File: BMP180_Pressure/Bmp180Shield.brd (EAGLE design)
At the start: 39.7 x 26.7 mm, 5 parts

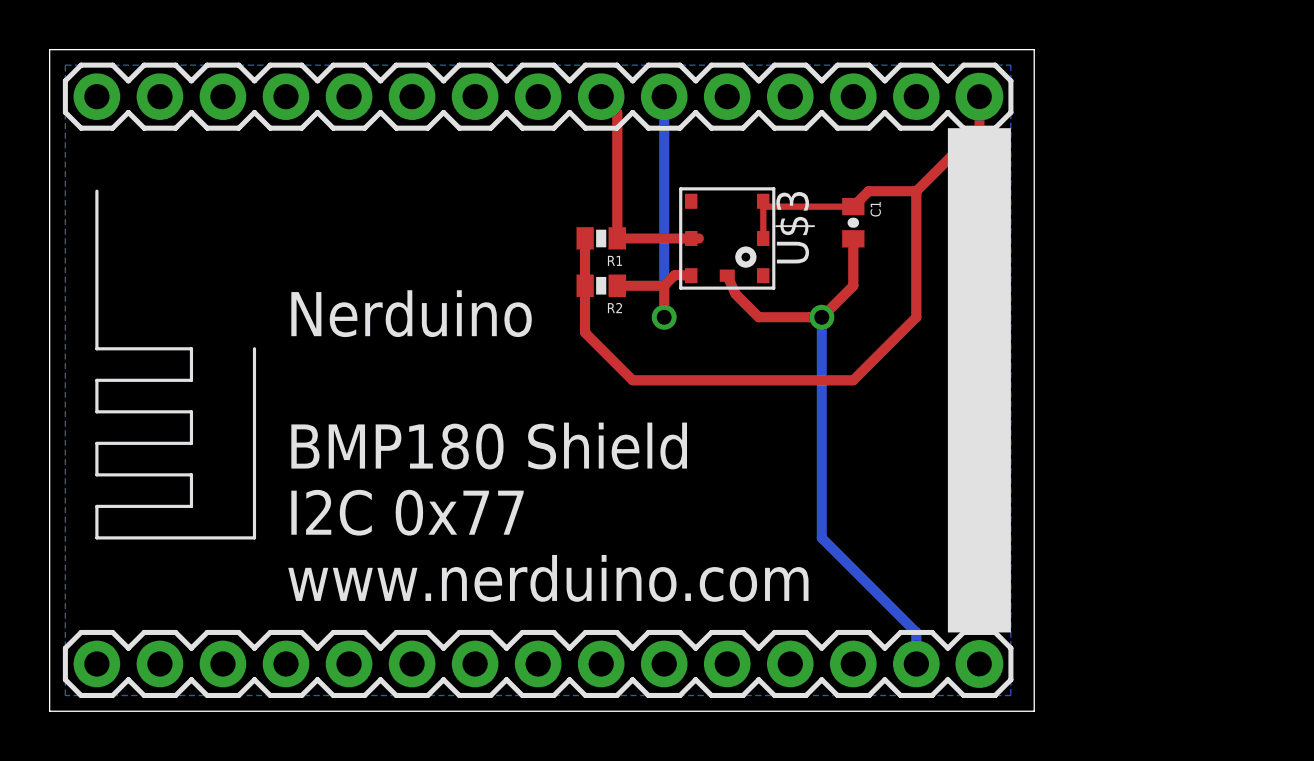
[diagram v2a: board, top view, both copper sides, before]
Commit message: Added OLED Shield Added LiPo Battery Charger Shield Updated outlines of all shields to match the cutout of the nodemcu board
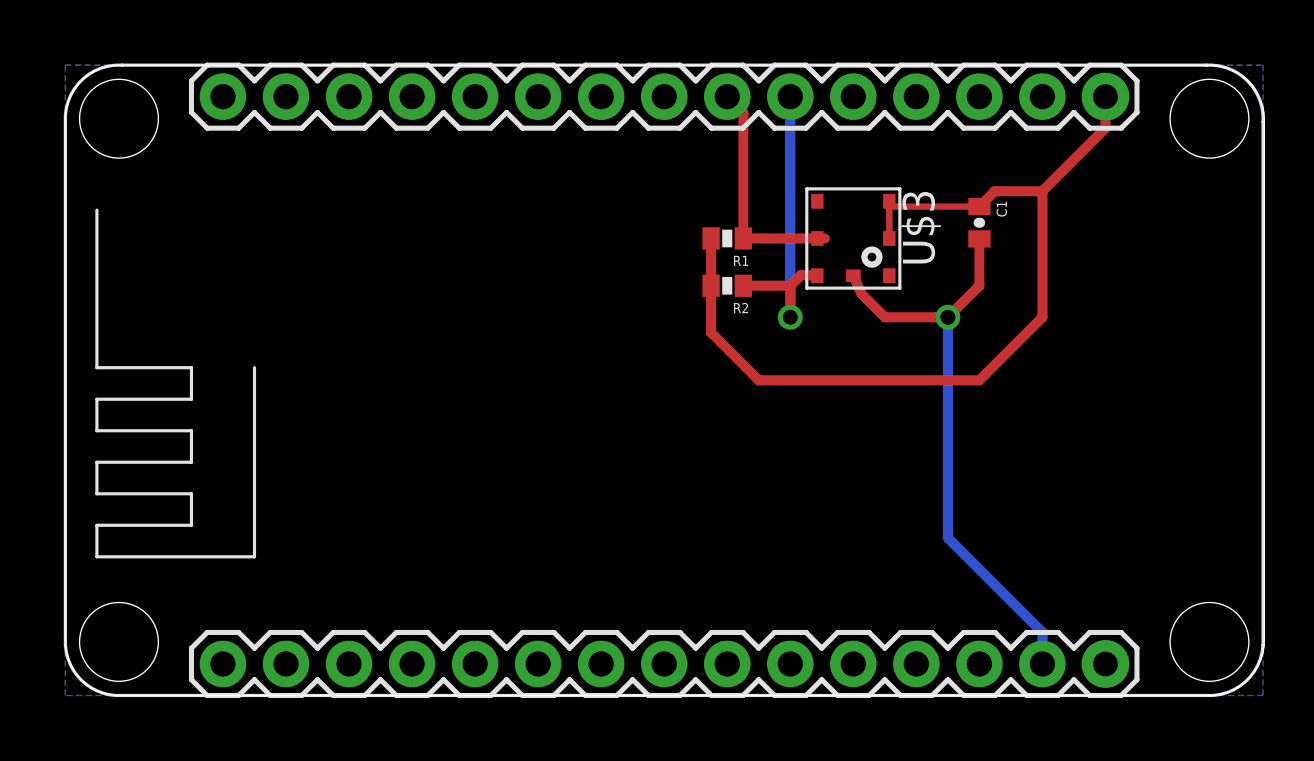
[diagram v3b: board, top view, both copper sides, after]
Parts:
- moved R1 5.08 mm to (26.7, 18.4)
- moved R2 5.08 mm to (26.7, 16.5)
- moved C1 5.08 mm to (36.8, 19.1)
- moved U$1 5.08 mm to (24.1, 6.35)
- moved U$3 5.08 mm to (31.8, 18.4)
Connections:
- net GND: now also U$1.10, U$1.17, U$1.24
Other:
- board size 39.7 x 26.7 mm -> 48.3 x 25.4 mm
- board text added: "NERDUINO BMP180 Shield I2C 0x77 www.nerduino.com"
- board text removed: "Nerduino BMP180 Shield I2C 0x77 www.nerduino.com"
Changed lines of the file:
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@@
 <setting verticaltext="up"/>
 </settings>
-<grid distance="0.025" unitdist="inch" unit="inch" style="lines" multiple="1" display="no" altdistance="0.0125" altunitdist="inch" altunit="inch"/>
+<grid distance="0.005" unitdist="inch" unit="inch" style="lines" multiple="1" display="no" altdistance="0.0125" altunitdist="inch" altunit="inch"/>
 <layers>
 <layer number="1" name="Top" color="4" fill="1" visible="yes" active="yes"/>
@@
 <board>
 <plain>
-<wire x1="-0.635" y1="-0.635" x2="39.04" y2="-0.635" width="0" layer="20"/>
-<wire x1="39.04" y1="-0.635" x2="39.04" y2="26.025" width="0" layer="20"/>
-<wire x1="39.04" y1="26.025" x2="-0.635" y2="26.025" width="0" layer="20"/>
-<wire x1="-0.635" y1="26.025" x2="-0.635" y2="-0.635" width="0" layer="20"/>
-<text x="8.89" y="3.81" size="1.778" layer="121">Nerduino
+<wire x1="0" y1="23.237253125" x2="0" y2="2.1849875" width="0" layer="20"/>
+<wire x1="0" y1="2.1849875" x2="2.1849875" y2="0" width="0" layer="20" curve="90"/>
+<wire x1="2.1849875" y1="0" x2="46.0843125" y2="0" width="0" layer="20"/>
+<wire x1="46.0843125" y1="0" x2="48.311" y2="2.2266875" width="0" layer="20" curve="90"/>
+<wire x1="48.311" y1="2.2266875" x2="48.311" y2="23.205321875" width="0" layer="20"/>
+<wire x1="48.311" y1="23.205321875" x2="46.126321875" y2="25.39" width="0" layer="20" curve="90"/>
+<wire x1="46.126321875" y1="25.39" x2="2.152746875" y2="25.39" width="0" layer="20"/>
+<wire x1="2.152746875" y1="25.39" x2="0" y2="23.237253125" width="0" layer="20" curve="90"/>
+<text x="32.385" y="3.683" size="1.778" layer="122" rot="MR0">NERDUINO
 BMP180 Shield
 I2C 0x77
@@
 </autorouter>
 <elements>
-<element name="C1" library="SparkFun" package="0402-CAP" value="0.1uF" x="31.75" y="19.05" rot="R270"/>
-<element name="R1" library="SparkFun" package="0402-RES" value="4.7k" x="21.59" y="18.415" rot="R180"/>
-<element name="R2" library="SparkFun" package="0402-RES" value="4.7k" x="21.59" y="16.51" rot="R180"/>
-<element name="U$1" library="NerduinoShieldLib" package="NERDUINO_STACK" value="NERDSHIELD" x="19.05" y="6.35"/>
-<element name="U$3" library="SparkFun-Sensors" package="BMP180" value="BMP180" x="26.67" y="18.415" rot="R270"/>
+<element name="C1" library="SparkFun" package="0402-CAP" value="0.1uF" x="36.83" y="19.05" rot="R270"/>
+<element name="R1" library="SparkFun" package="0402-RES" value="4.7k" x="26.67" y="18.415" rot="R180"/>
+<element name="R2" library="SparkFun" package="0402-RES" value="4.7k" x="26.67" y="16.51" rot="R180"/>
+<element name="U$1" library="NerduinoShieldLib" package="NERDUINO_STACK" value="NERDSHIELD" x="24.13" y="6.35"/>
+<element name="U$3" library="SparkFun-Sensors" package="BMP180" value="BMP180" x="31.75" y="18.415" rot="R270"/>
 </elements>
 <signals>
@@
 <polygon width="0.4064" layer="16">
 <vertex x="0" y="25.4"/>
-<vertex x="38.1" y="25.4"/>
-<vertex x="38.1" y="0"/>
+<vertex x="48.26" y="25.4"/>
+<vertex x="48.26" y="0"/>
 <vertex x="0" y="0"/>
 </polygon>
-<wire x1="31.75" y1="18.4" x2="31.75" y2="16.51" width="0.4064" layer="1"/>
-<wire x1="31.75" y1="16.51" x2="30.48" y2="15.24" width="0.4064" layer="1"/>
-<wire x1="30.48" y1="15.24" x2="30.005" y2="15.24" width="0.4064" layer="1"/>
-<via x="30.48" y="15.24" extent="1-16" drill="0.6" shape="square"/>
-<wire x1="30.48" y1="15.24" x2="30.48" y2="6.35" width="0.4064" layer="16"/>
-<wire x1="30.48" y1="6.35" x2="34.29" y2="2.54" width="0.4064" layer="16"/>
-<wire x1="34.29" y1="2.54" x2="34.29" y2="1.27" width="0.4064" layer="16"/>
+<wire x1="36.83" y1="18.4" x2="36.83" y2="16.51" width="0.4064" layer="1"/>
+<wire x1="36.83" y1="16.51" x2="35.56" y2="15.24" width="0.4064" layer="1"/>
+<wire x1="35.56" y1="15.24" x2="35.085" y2="15.24" width="0.4064" layer="1"/>
+<via x="35.56" y="15.24" extent="1-16" drill="0.6" shape="square"/>
+<wire x1="35.56" y1="15.24" x2="35.56" y2="6.35" width="0.4064" layer="16"/>
+<wire x1="35.56" y1="6.35" x2="39.37" y2="2.54" width="0.4064" layer="16"/>
+<wire x1="39.37" y1="2.54" x2="39.37" y2="1.27" width="0.4064" layer="16"/>
 <contactref element="U$3" pad="7"/>
-<wire x1="26.67" y1="16.915" x2="27.005" y2="16.175" width="0.4064" layer="1"/>
-<wire x1="27.005" y1="16.175" x2="27.94" y2="15.24" width="0.4064" layer="1"/>
-<wire x1="27.94" y1="15.24" x2="30.48" y2="15.24" width="0.4064" layer="1"/>
+<wire x1="31.75" y1="16.915" x2="32.085" y2="16.175" width="0.4064" layer="1"/>
+<wire x1="32.085" y1="16.175" x2="33.02" y2="15.24" width="0.4064" layer="1"/>
+<wire x1="33.02" y1="15.24" x2="35.56" y2="15.24" width="0.4064" layer="1"/>
+<contactref element="U$1" pad="10"/>
+<contactref element="U$1" pad="17"/>
+<contactref element="U$1" pad="24"/>
 </signal>
 <signal name="3.3V">
@@
 <contactref element="R2" pad="2"/>
 <contactref element="R1" pad="2"/>
-<wire x1="36.83" y1="24.13" x2="36.83" y2="22.86" width="0.4064" layer="1"/>
-<wire x1="36.83" y1="22.86" x2="34.29" y2="20.32" width="0.4064" layer="1"/>
-<wire x1="34.29" y1="20.32" x2="32.37" y2="20.32" width="0.4064" layer="1"/>
-<wire x1="32.37" y1="20.32" x2="31.75" y2="19.7" width="0.4064" layer="1"/>
-<wire x1="20.94" y1="18.415" x2="20.94" y2="16.51" width="0.4064" layer="1"/>
-<wire x1="20.94" y1="16.51" x2="20.94" y2="14.62" width="0.4064" layer="1"/>
-<wire x1="20.94" y1="14.62" x2="22.86" y2="12.7" width="0.4064" layer="1"/>
-<wire x1="22.86" y1="12.7" x2="31.75" y2="12.7" width="0.4064" layer="1"/>
-<wire x1="31.75" y1="12.7" x2="34.29" y2="15.24" width="0.4064" layer="1"/>
-<wire x1="34.29" y1="15.24" x2="34.29" y2="20.32" width="0.4064" layer="1"/>
+<wire x1="41.91" y1="24.13" x2="41.91" y2="22.86" width="0.4064" layer="1"/>
+<wire x1="41.91" y1="22.86" x2="39.37" y2="20.32" width="0.4064" layer="1"/>
+<wire x1="39.37" y1="20.32" x2="37.45" y2="20.32" width="0.4064" layer="1"/>
+<wire x1="37.45" y1="20.32" x2="36.83" y2="19.7" width="0.4064" layer="1"/>
+<wire x1="26.02" y1="18.415" x2="26.02" y2="16.51" width="0.4064" layer="1"/>
+<wire x1="26.02" y1="16.51" x2="26.02" y2="14.62" width="0.4064" layer="1"/>
+<wire x1="26.02" y1="14.62" x2="27.94" y2="12.7" width="0.4064" layer="1"/>
+<wire x1="27.94" y1="12.7" x2="36.83" y2="12.7" width="0.4064" layer="1"/>
+<wire x1="36.83" y1="12.7" x2="39.37" y2="15.24" width="0.4064" layer="1"/>
+<wire x1="39.37" y1="15.24" x2="39.37" y2="20.32" width="0.4064" layer="1"/>
 <contactref element="U$3" pad="2"/>
 <contactref element="U$3" pad="3"/>
-<wire x1="31.75" y1="19.7" x2="28.12" y2="19.7" width="0.254" layer="1"/>
-<wire x1="28.12" y1="19.7" x2="28.12" y2="19.915" width="0.254" layer="1"/>
-<wire x1="28.12" y1="19.915" x2="28.12" y2="18.415" width="0.254" layer="1"/>
+<wire x1="36.83" y1="19.7" x2="33.2" y2="19.7" width="0.254" layer="1"/>
+<wire x1="33.2" y1="19.7" x2="33.2" y2="19.915" width="0.254" layer="1"/>
+<wire x1="33.2" y1="19.915" x2="33.2" y2="18.415" width="0.254" layer="1"/>
 </signal>
 <signal name="N$2">
 <contactref element="R2" pad="1"/>
 <contactref element="U$1" pad="21"/>
-<wire x1="24.13" y1="16.51" x2="22.24" y2="16.51" width="0.4064" layer="1"/>
-<wire x1="24.13" y1="24.13" x2="24.13" y2="15.24" width="0.4064" layer="16"/>
-<via x="24.13" y="15.24" extent="1-16" drill="0.6" shape="square"/>
-<wire x1="24.13" y1="15.24" x2="24.13" y2="16.51" width="0.4064" layer="1"/>
+<wire x1="29.21" y1="16.51" x2="27.32" y2="16.51" width="0.4064" layer="1"/>
+<wire x1="29.21" y1="24.13" x2="29.21" y2="15.24" width="0.4064" layer="16"/>
+<via x="29.21" y="15.24" extent="1-16" drill="0.6" shape="square"/>
+<wire x1="29.21" y1="15.24" x2="29.21" y2="16.51" width="0.4064" layer="1"/>
 <contactref element="U$3" pad="6"/>
-<wire x1="25.22" y1="16.915" x2="24.565" y2="16.945" width="0.4064" layer="1"/>
-<wire x1="24.565" y1="16.945" x2="24.13" y2="16.51" width="0.4064" layer="1"/>
+<wire x1="30.3" y1="16.915" x2="29.645" y2="16.945" width="0.4064" layer="1"/>
+<wire x1="29.645" y1="16.945" x2="29.21" y2="16.51" width="0.4064" layer="1"/>
 </signal>
 <signal name="N$3">
 <contactref element="R1" pad="1"/>
 <contactref element="U$1" pad="22"/>
-<wire x1="22.24" y1="18.415" x2="22.24" y2="23.48" width="0.4064" layer="1"/>
-<wire x1="22.24" y1="23.48" x2="21.59" y2="24.13" width="0.4064" layer="1"/>
+<wire x1="27.32" y1="18.415" x2="27.32" y2="23.48" width="0.4064" layer="1"/>
+<wire x1="27.32" y1="23.48" x2="26.67" y2="24.13" width="0.4064" layer="1"/>
 <contactref element="U$3" pad="5"/>
-<wire x1="22.24" y1="18.415" x2="25.22" y2="18.415" width="0.4064" layer="1"/>
-<wire x1="25.525" y1="18.415" x2="25.22" y2="18.415" width="0.4064" layer="1"/>
+<wire x1="27.32" y1="18.415" x2="30.3" y2="18.415" width="0.4064" layer="1"/>
+<wire x1="30.605" y1="18.415" x2="30.3" y2="18.415" width="0.4064" layer="1"/>
 </signal>
 </signals>

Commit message: Updated the i2c pins to all shields to use d11/d12  as these pins will have dual use with the upcoming wifimcu Added FM24W256  Fram shield Added X95840 Digital potentiometer Shield Added AD5696 DAC Shield
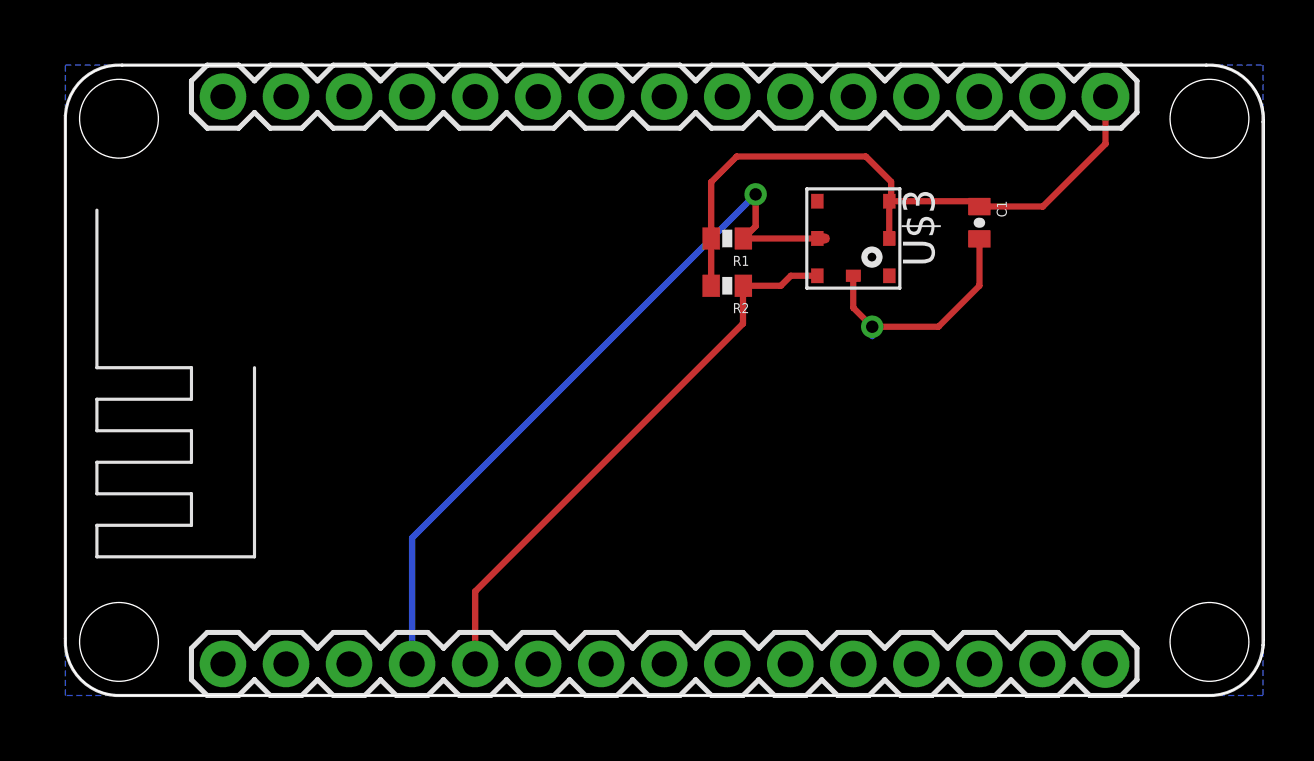
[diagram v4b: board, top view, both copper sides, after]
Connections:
- net GND: no longer U$1.24
- net N$2: now also U$1.5; no longer U$1.21
- net N$3: now also U$1.4; no longer U$1.22
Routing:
- net N$3: track 9.27 -> 29.9 mm, vias 0 -> 1
- net GND: track 24.4 -> 9.64 mm
- net 3.3V: track 37.1 -> 26.3 mm
- net N$2: track 13.3 -> 23.0 mm, vias 1 -> 0
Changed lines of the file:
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@@
 <vertex x="0" y="0"/>
 </polygon>
-<wire x1="36.83" y1="18.4" x2="36.83" y2="16.51" width="0.4064" layer="1"/>
-<wire x1="36.83" y1="16.51" x2="35.56" y2="15.24" width="0.4064" layer="1"/>
-<wire x1="35.56" y1="15.24" x2="35.085" y2="15.24" width="0.4064" layer="1"/>
-<via x="35.56" y="15.24" extent="1-16" drill="0.6" shape="square"/>
-<wire x1="35.56" y1="15.24" x2="35.56" y2="6.35" width="0.4064" layer="16"/>
-<wire x1="35.56" y1="6.35" x2="39.37" y2="2.54" width="0.4064" layer="16"/>
-<wire x1="39.37" y1="2.54" x2="39.37" y2="1.27" width="0.4064" layer="16"/>
 <contactref element="U$3" pad="7"/>
-<wire x1="31.75" y1="16.915" x2="32.085" y2="16.175" width="0.4064" layer="1"/>
-<wire x1="32.085" y1="16.175" x2="33.02" y2="15.24" width="0.4064" layer="1"/>
-<wire x1="33.02" y1="15.24" x2="35.56" y2="15.24" width="0.4064" layer="1"/>
 <contactref element="U$1" pad="10"/>
 <contactref element="U$1" pad="17"/>
-<contactref element="U$1" pad="24"/>
+<wire x1="31.75" y1="16.915" x2="31.75" y2="15.621" width="0.254" layer="1"/>
+<wire x1="31.75" y1="15.621" x2="32.512" y2="14.859" width="0.254" layer="1"/>
+<via x="32.512" y="14.859" extent="1-16" drill="0.5"/>
+<wire x1="32.512" y1="14.859" x2="32.512" y2="14.478" width="0.254" layer="16"/>
+<wire x1="36.83" y1="18.4" x2="36.83" y2="16.51" width="0.254" layer="1"/>
+<wire x1="36.83" y1="16.51" x2="35.179" y2="14.859" width="0.254" layer="1"/>
+<wire x1="35.179" y1="14.859" x2="32.512" y2="14.859" width="0.254" layer="1"/>
 </signal>
 <signal name="3.3V">
@@
 <contactref element="R2" pad="2"/>
 <contactref element="R1" pad="2"/>
-<wire x1="41.91" y1="24.13" x2="41.91" y2="22.86" width="0.4064" layer="1"/>
-<wire x1="41.91" y1="22.86" x2="39.37" y2="20.32" width="0.4064" layer="1"/>
-<wire x1="39.37" y1="20.32" x2="37.45" y2="20.32" width="0.4064" layer="1"/>
-<wire x1="37.45" y1="20.32" x2="36.83" y2="19.7" width="0.4064" layer="1"/>
-<wire x1="26.02" y1="18.415" x2="26.02" y2="16.51" width="0.4064" layer="1"/>
-<wire x1="26.02" y1="16.51" x2="26.02" y2="14.62" width="0.4064" layer="1"/>
-<wire x1="26.02" y1="14.62" x2="27.94" y2="12.7" width="0.4064" layer="1"/>
-<wire x1="27.94" y1="12.7" x2="36.83" y2="12.7" width="0.4064" layer="1"/>
-<wire x1="36.83" y1="12.7" x2="39.37" y2="15.24" width="0.4064" layer="1"/>
-<wire x1="39.37" y1="15.24" x2="39.37" y2="20.32" width="0.4064" layer="1"/>
 <contactref element="U$3" pad="2"/>
 <contactref element="U$3" pad="3"/>
-<wire x1="36.83" y1="19.7" x2="33.2" y2="19.7" width="0.254" layer="1"/>
-<wire x1="33.2" y1="19.7" x2="33.2" y2="19.915" width="0.254" layer="1"/>
 <wire x1="33.2" y1="19.915" x2="33.2" y2="18.415" width="0.254" layer="1"/>
+<wire x1="33.2" y1="19.915" x2="36.615" y2="19.915" width="0.254" layer="1"/>
+<wire x1="36.615" y1="19.915" x2="36.83" y2="19.7" width="0.254" layer="1"/>
+<wire x1="36.83" y1="19.7" x2="39.385" y2="19.7" width="0.254" layer="1"/>
+<wire x1="39.385" y1="19.7" x2="41.91" y2="22.225" width="0.254" layer="1"/>
+<wire x1="41.91" y1="22.225" x2="41.91" y2="24.13" width="0.254" layer="1"/>
+<wire x1="26.02" y1="18.415" x2="26.02" y2="20.686" width="0.254" layer="1"/>
+<wire x1="26.02" y1="20.686" x2="27.051" y2="21.717" width="0.254" layer="1"/>
+<wire x1="27.051" y1="21.717" x2="32.258" y2="21.717" width="0.254" layer="1"/>
+<wire x1="32.258" y1="21.717" x2="33.274" y2="20.701" width="0.254" layer="1"/>
+<wire x1="33.274" y1="20.701" x2="33.274" y2="19.989" width="0.254" layer="1"/>
+<wire x1="33.274" y1="19.989" x2="33.2" y2="19.915" width="0.254" layer="1"/>
+<wire x1="26.02" y1="18.415" x2="26.02" y2="16.51" width="0.254" layer="1"/>
 </signal>
 <signal name="N$2">
 <contactref element="R2" pad="1"/>
-<contactref element="U$1" pad="21"/>
-<wire x1="29.21" y1="16.51" x2="27.32" y2="16.51" width="0.4064" layer="1"/>
-<wire x1="29.21" y1="24.13" x2="29.21" y2="15.24" width="0.4064" layer="16"/>
-<via x="29.21" y="15.24" extent="1-16" drill="0.6" shape="square"/>
-<wire x1="29.21" y1="15.24" x2="29.21" y2="16.51" width="0.4064" layer="1"/>
 <contactref element="U$3" pad="6"/>
-<wire x1="30.3" y1="16.915" x2="29.645" y2="16.945" width="0.4064" layer="1"/>
-<wire x1="29.645" y1="16.945" x2="29.21" y2="16.51" width="0.4064" layer="1"/>
+<contactref element="U$1" pad="5"/>
+<wire x1="30.3" y1="16.915" x2="29.234" y2="16.915" width="0.254" layer="1"/>
+<wire x1="29.234" y1="16.915" x2="28.829" y2="16.51" width="0.254" layer="1"/>
+<wire x1="28.829" y1="16.51" x2="27.32" y2="16.51" width="0.254" layer="1"/>
+<wire x1="16.51" y1="1.27" x2="16.51" y2="4.191" width="0.254" layer="1"/>
+<wire x1="16.51" y1="4.191" x2="27.305" y2="14.986" width="0.254" layer="1"/>
+<wire x1="27.305" y1="14.986" x2="27.305" y2="16.129" width="0.254" layer="1"/>
+<wire x1="27.305" y1="16.129" x2="27.432" y2="16.256" width="0.254" layer="1"/>
+<wire x1="27.432" y1="16.256" x2="27.432" y2="16.398" width="0.254" layer="1"/>
+<wire x1="27.432" y1="16.398" x2="27.32" y2="16.51" width="0.254" layer="1"/>
 </signal>
 <signal name="N$3">
 <contactref element="R1" pad="1"/>
-<contactref element="U$1" pad="22"/>
-<wire x1="27.32" y1="18.415" x2="27.32" y2="23.48" width="0.4064" layer="1"/>
-<wire x1="27.32" y1="23.48" x2="26.67" y2="24.13" width="0.4064" layer="1"/>
 <contactref element="U$3" pad="5"/>
-<wire x1="27.32" y1="18.415" x2="30.3" y2="18.415" width="0.4064" layer="1"/>
 <wire x1="30.605" y1="18.415" x2="30.3" y2="18.415" width="0.4064" layer="1"/>
+<contactref element="U$1" pad="4"/>
+<wire x1="30.3" y1="18.415" x2="27.32" y2="18.415" width="0.254" layer="1"/>
+<wire x1="13.97" y1="1.27" x2="13.97" y2="6.35" width="0.254" layer="16"/>
+<wire x1="13.97" y1="6.35" x2="27.813" y2="20.193" width="0.254" layer="16"/>
+<via x="27.813" y="20.193" extent="1-16" drill="0.5"/>
+<wire x1="27.813" y1="20.193" x2="27.813" y2="18.908" width="0.254" layer="1"/>
+<wire x1="27.813" y1="18.908" x2="27.32" y2="18.415" width="0.254" layer="1"/>
 </signal>
 </signals>
